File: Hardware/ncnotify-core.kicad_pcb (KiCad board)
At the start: 4 copper layers, 47.5 x 24 mm, 42 parts, among them J1 5-1634503-1, J2 TC2030-CTX, J3 USB4110-GF-A, Q1 NX3008NBKS, SW1 SW_Push, SW2 SW_Push, U1 STM32L422CBT6, U2 TLV71333PDBV, U3 USBLC6-2SC6, U4 USBLC6-2SC6, X1 SMTU1632-LF, Y1 Q13FC1350000400

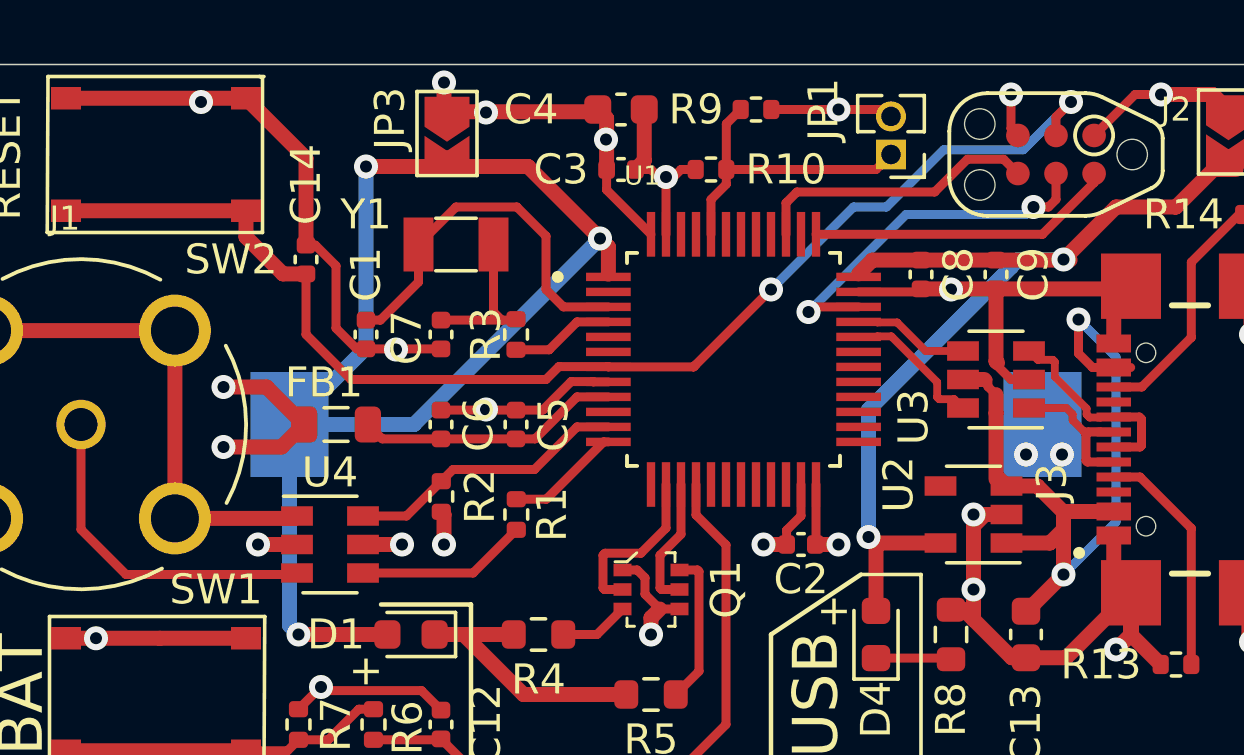
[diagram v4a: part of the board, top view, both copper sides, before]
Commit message: Cleanup silkscreen, add part numbers to sch bom
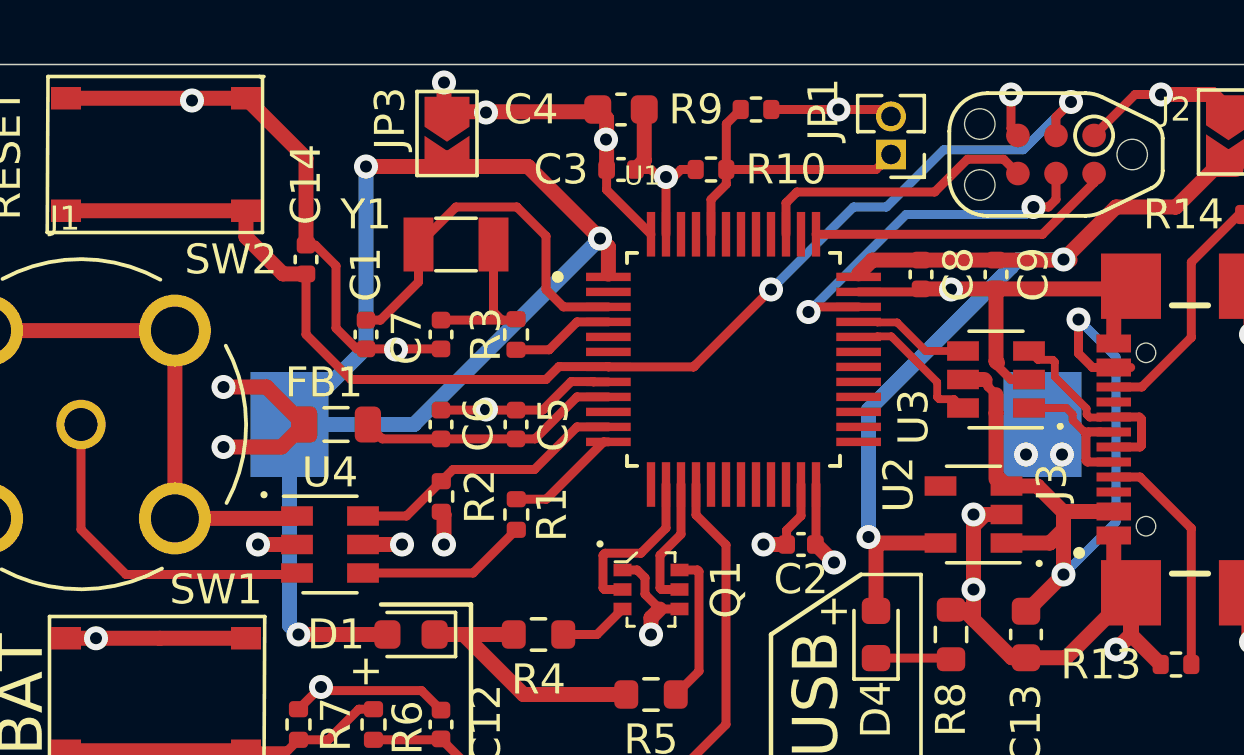
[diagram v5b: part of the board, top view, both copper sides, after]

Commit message: bump to developing version v1.1
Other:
- board text added: "NCNotify Data Logger Bowen Shaner v1.1"
- board text removed: "NCNotify Data Logger Bowen Shaner v1.0"

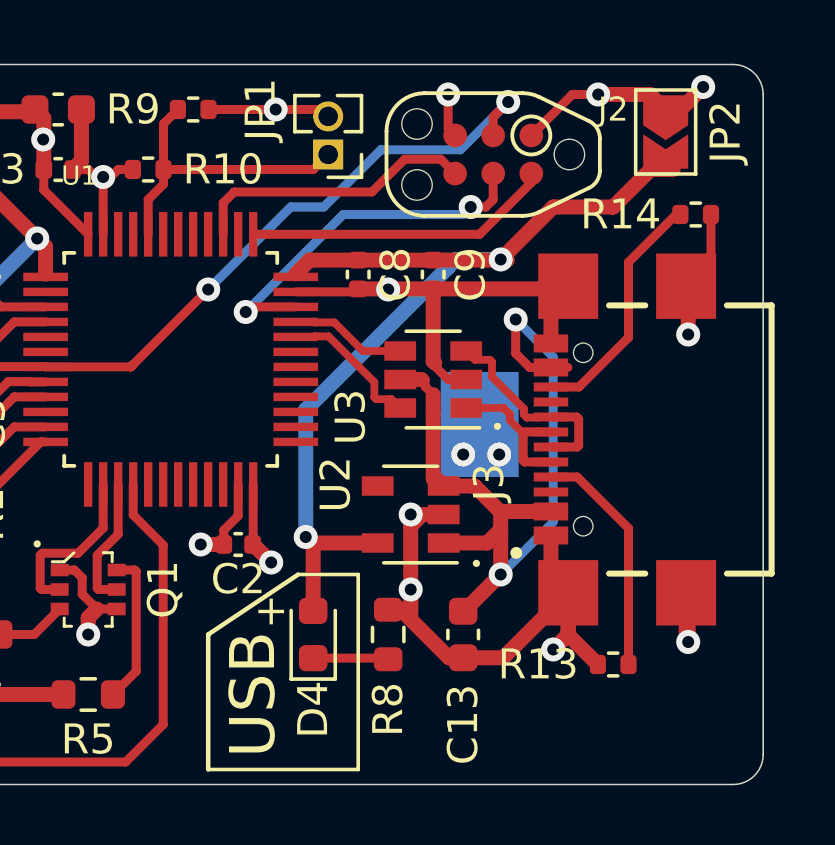
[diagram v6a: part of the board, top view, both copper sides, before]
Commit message: Fix SWD CLK/DIO pin swap, add UART test points
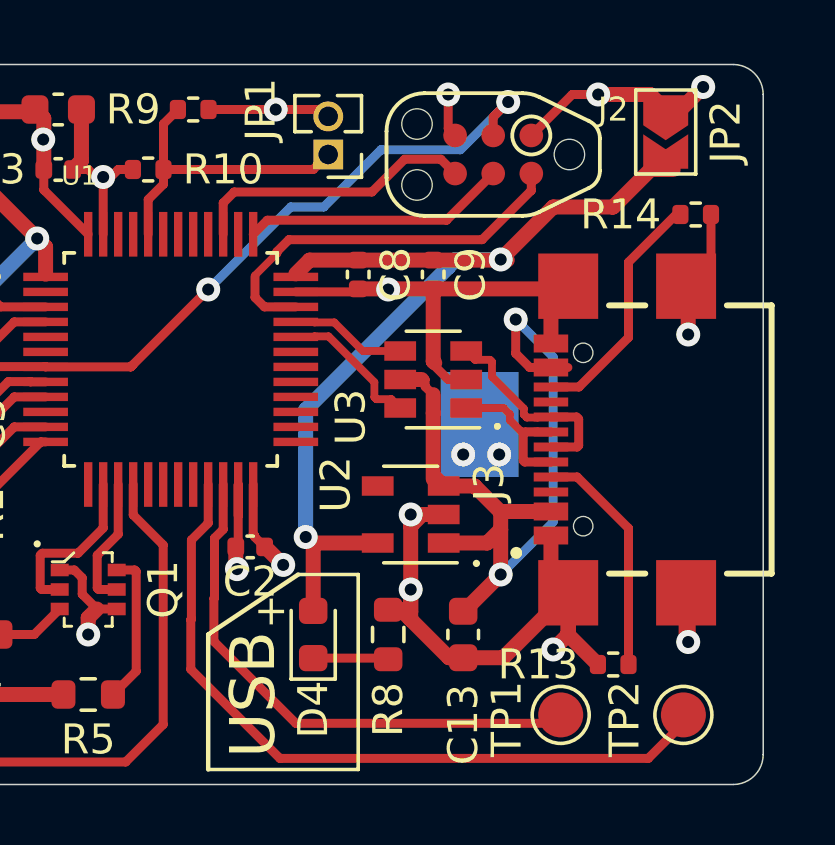
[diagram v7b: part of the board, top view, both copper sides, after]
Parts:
- added TP1: TestPoint, TestPoint:TestPoint_Pad_D1.5mm, F.Cu at (246.2, -28.3)
- added TP2: TestPoint, TestPoint:TestPoint_Pad_D1.5mm, F.Cu at (250.3, -28.3)
- moved C2 0.41 mm to (235.9, -33.9)
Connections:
- J2 pad 2: JTCK-SWCLK -> JTMS-SWDIO
- J2 pad 4: JTMS-SWDIO -> JTCK-SWCLK
- U1 pad 21: Net-(U1-Pad21) -> USART3_TX
- U1 pad 22: Net-(U1-Pad22) -> USART3_RX
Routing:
- net USART3_TX: track 0.00 -> 24.5 mm
- net USART3_RX: track 0.00 -> 18.1 mm
- net JTCK-SWCLK: track 10.3 -> 8.84 mm
- net JTMS-SWDIO: track 12.4 -> 13.5 mm, vias 2 -> 0
- net GND: track 97.3 -> 98.3 mm
- net VDD: track 38.3 -> 39.1 mm

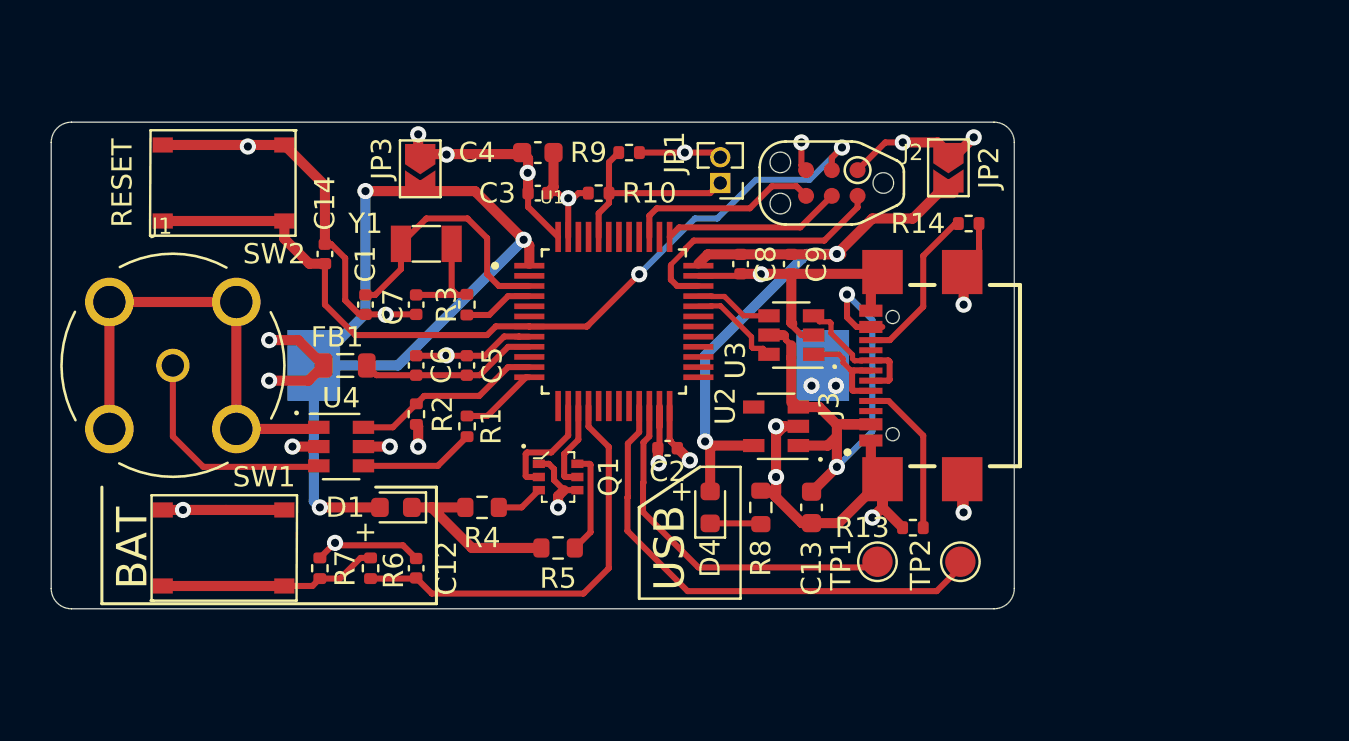
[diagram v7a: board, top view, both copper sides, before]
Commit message: Board shrink; swap to RA BNC mount
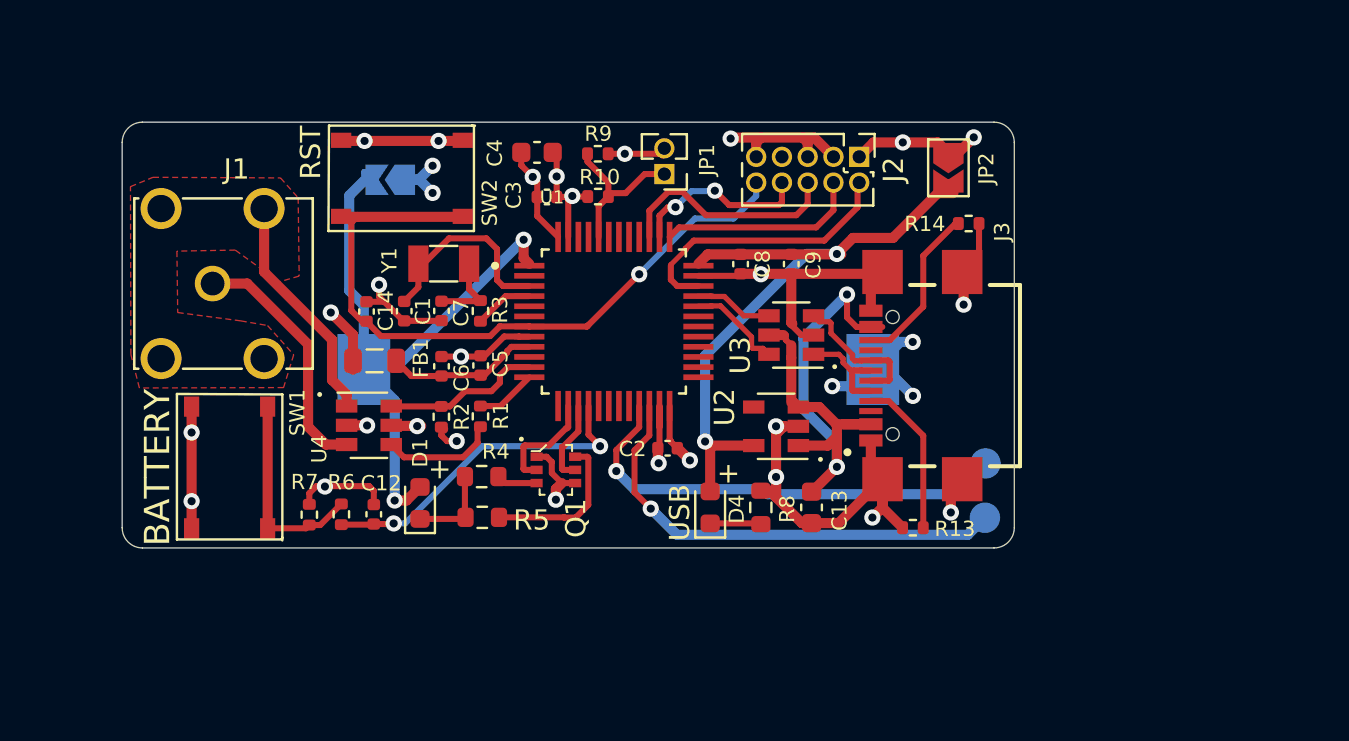
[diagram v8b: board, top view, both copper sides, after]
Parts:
- J1: value 5-1634503-1 -> BNC5-J-P-GN-RA-BH2D; footprint libs:TE_5-1634503-1 -> libs:SAMTEC_BNC5-J-P-GN-RA-BH2D
- J2: value TC2030-CTX -> Conn_ARM_JTAG_SWD_10; footprint libs:TC2030-IDC-NL -> Connector_PinHeader_1.27mm:PinHeader_2x05_P1.27mm_Vertical
- JP3, TP1, TP2: moved to B.Cu
- moved SW2 8.80 mm to (222.8, -47.2)
- moved TP1 5.73 mm to (251.6, -30.5), turned to 90 degrees
- moved TP2 5.01 mm to (251.6, -33.2), turned to 270 degrees
- moved J1 4.49 mm to (213.5, -42.0), turned to 270 degrees
- moved R5 4.03 mm to (226.8, -30.5)
- moved SW1 3.98 mm to (214.3, -33.0), turned to 90 degrees
- moved C14 3.50 mm to (221.1, -40.7)
- moved C12 3.38 mm to (221.4, -30.7)
- moved R6 3.02 mm to (219.8, -30.7)
- moved JP1 2.79 mm to (235.7, -47.4)
- moved R7 2.69 mm to (218.2, -30.6)
- moved X1 2.48 mm to (233.5, -37.8)
- moved C1 1.94 mm to (222.9, -40.7)
- moved J2 1.87 mm to (245.3, -48.3), turned to 270 degrees
- moved U4 1.73 mm to (221.2, -35.0)
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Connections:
- J2 pad 3: NRST -> GND
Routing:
- net VBAT: track 45.4 -> 31.5 mm, vias 3 -> 2
- net S-: track 23.8 -> 11.4 mm
- net JTDI: track 0.00 -> 8.91 mm, vias 0 -> 2
- net NRST: track 42.8 -> 34.9 mm, vias 2 -> 1
- net VDD: track 39.1 -> 32.1 mm
- net USART3_RX: track 18.1 -> 23.1 mm, vias 0 -> 1
- net Net-(D1-Pad1): track 8.89 -> 4.30 mm
- net STATUS_READ: track 21.0 -> 16.6 mm, vias 0 -> 2
- net GND: track 98.3 -> 95.1 mm, vias 18 -> 21
- net OSC+: track 12.8 -> 10.0 mm
- net Net-(Q1-Pad6): track 5.09 -> 7.67 mm
- net Net-(JP1-Pad1): track 10.3 -> 7.84 mm
- net GPIO_S-: track 9.41 -> 7.65 mm
- net JTDO: track 9.58 -> 11.2 mm
- net USART3_TX: track 24.5 -> 23.0 mm, vias 0 -> 1
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- added copper zone on F.Cu, net S-
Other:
- board size 47.5 x 24 mm -> 44 x 21 mm
- board text added: "BATTERY"
- board text added: "NCNotify Data Logger v1.1 Bowen Shaner"
- board text added: "RST"
- board text added: "RX"
- board text added: "TX"
- board text removed: "BAT"
- board text removed: "NCNotify Data Logger Bowen Shaner v1.1"
- board text removed: "RESET"
